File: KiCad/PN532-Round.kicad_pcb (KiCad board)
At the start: 2 copper layers, 46 x 46 mm, 52 parts, among them J1 Bell, J2 Bell, J3 0.1", SW1 TAMPER, U1 PN532, U2 QR, Y1 27.12MHz

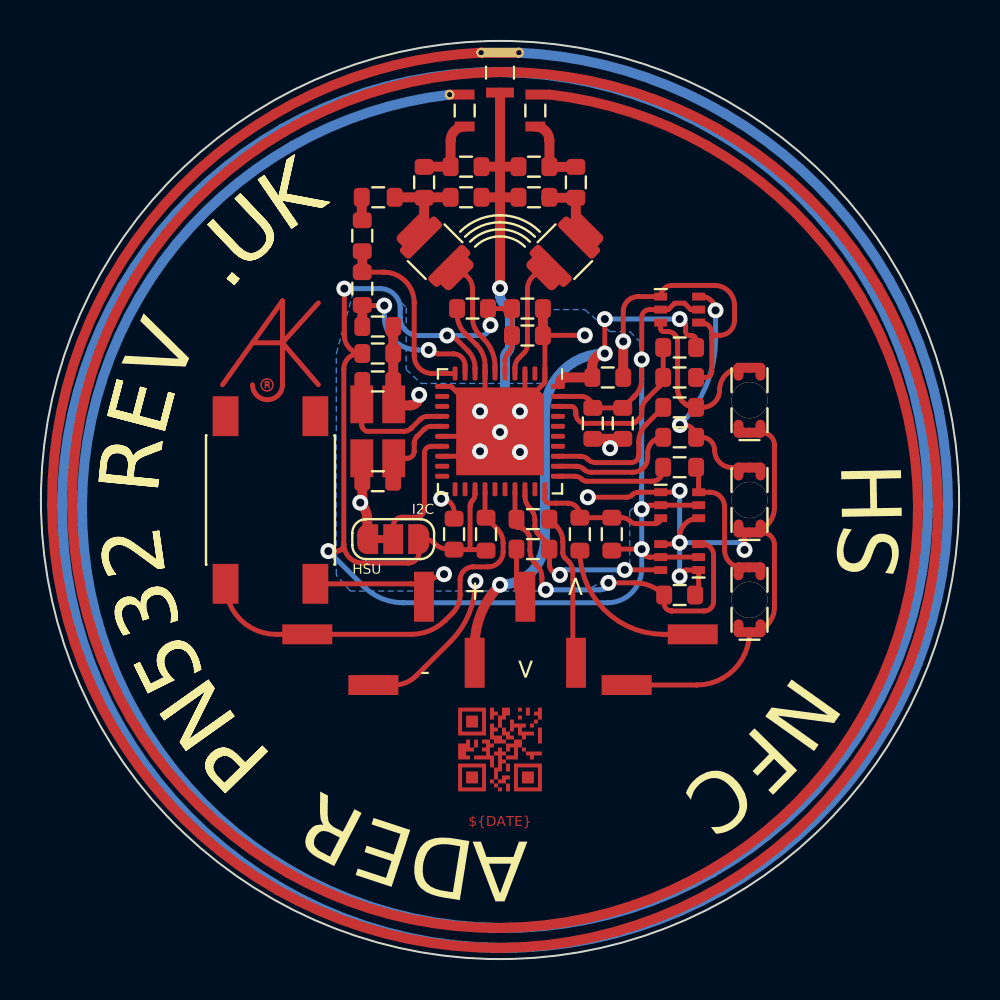
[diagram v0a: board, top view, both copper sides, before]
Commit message: Proper tamper switch
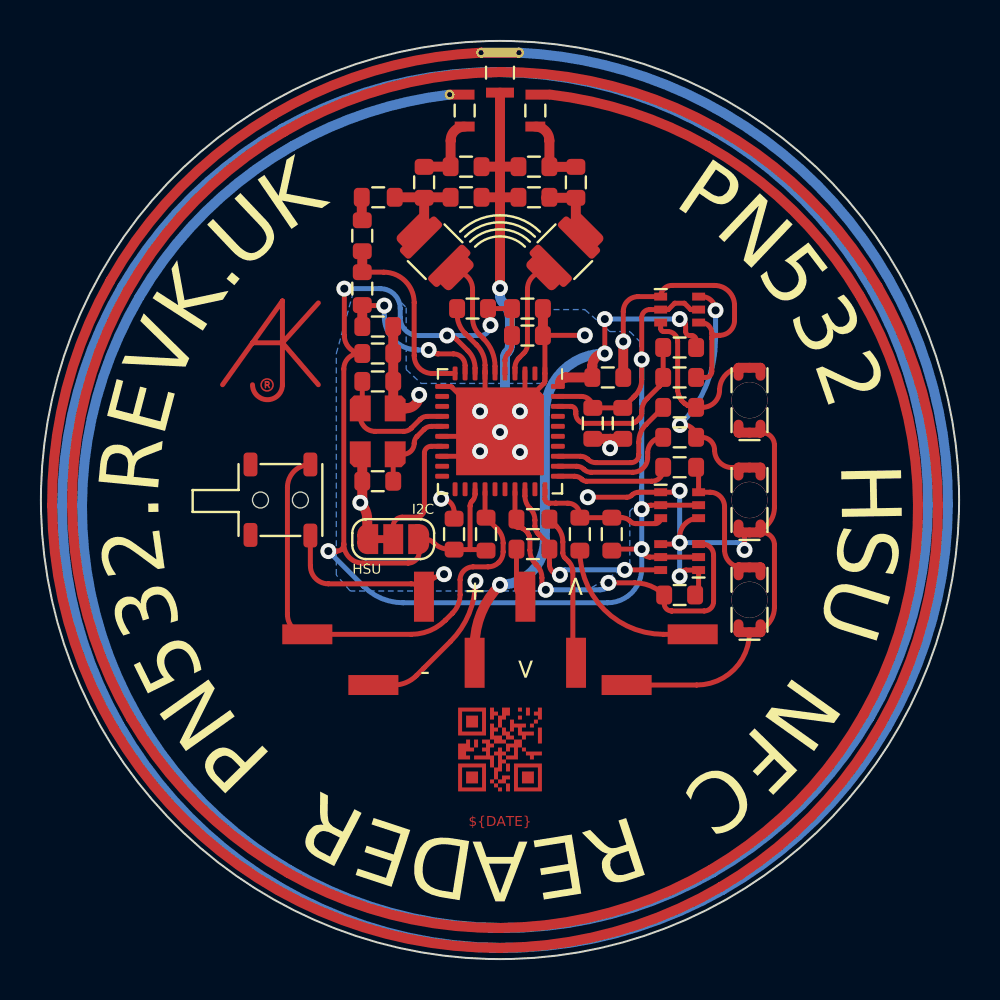
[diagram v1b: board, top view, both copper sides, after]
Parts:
- SW1: value TAMPER -> ESE13V01D; footprint RevK:SW_PUSH_6mm_SMD -> RevK:ESE13
- Y1: footprint RevK:Crystal-3.4x2.7 -> RevK:Crystal-3.2x2.5
- moved SW1 0.50 mm to (89.0, 100.0), turned to 180 degrees
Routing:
- net Net-(J2-Pad2): track 21.1 -> 25.3 mm
- net GND: track 125.4 -> 129.3 mm
- net Net-(C16-Pad1): track 5.48 -> 6.57 mm
- net Net-(C17-Pad1): track 3.43 -> 4.47 mm

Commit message: Revised layout (tamper)
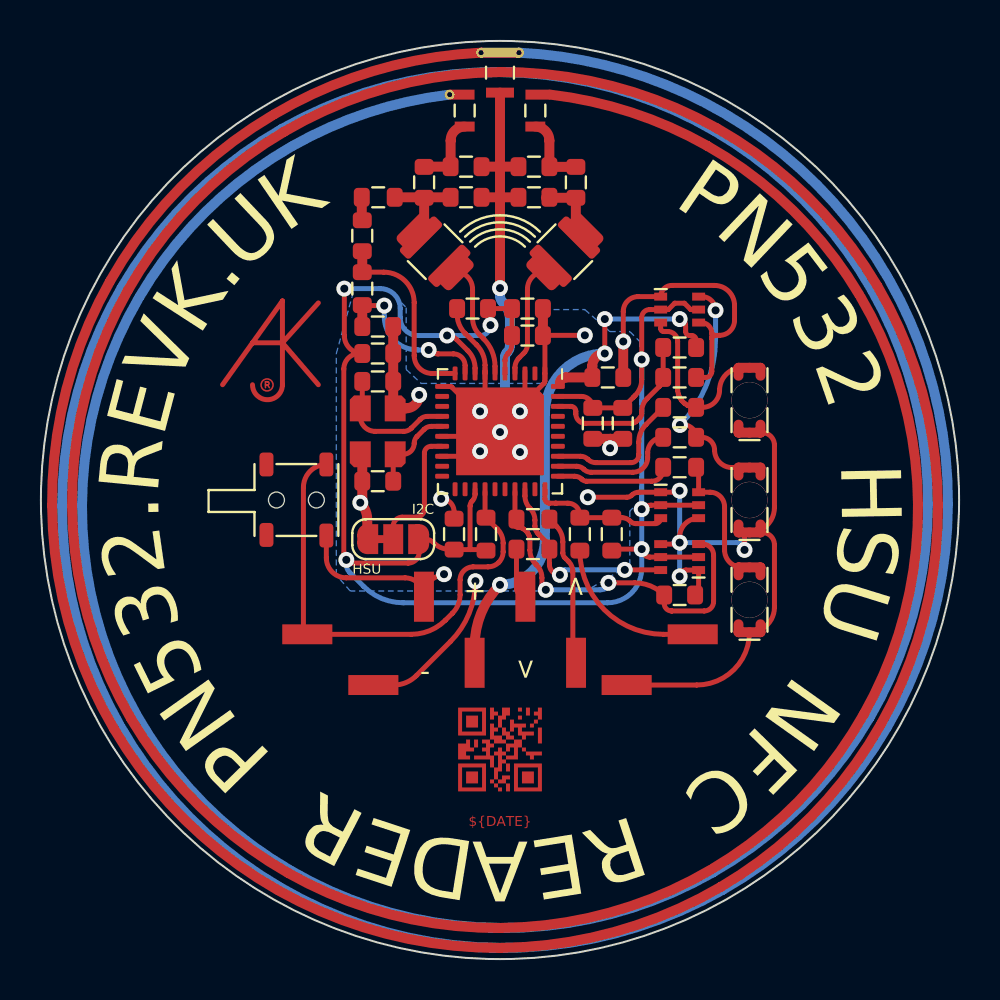
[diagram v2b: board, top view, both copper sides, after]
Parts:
- moved SW1 0.80 mm to (89.8, 100.0)
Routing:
- net +3V3: track 90.9 -> 89.4 mm
- net GND: track 129.3 -> 128.3 mm
